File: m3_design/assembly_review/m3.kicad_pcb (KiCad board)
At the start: 4 copper layers, 46 x 193 mm, 232 parts, among them J1 BAT+ / GND / SW / SW, J120 ARM CH2: RAW / BUS2, J121 IGNITER 1: E1- / E1+, J122 SERVO 3x4, J123 PULL-PIN PH 1x2, J124 ARM CH1: BUS1 / RAW, J125 IGNITER 2: E2+ / E2-, J2 SWD 1x6, J3 USB-C 2.0, J9 CAM 5V / GND / RX / TX, Q120 AON6403, Q121 AON6403, Q122 AO3400A, Q123 AO3400A, Q124 AON7524, Q125 AON7524, U1 STM32H743VIT6, U10 TPS2553DBVR, U11 TPS2121RUXR, U12 TXU0202DCUR, U13 TPS70933DBVR, U2 AP63203WU-7, U3 W25Q128JVSIQ, U4 LSM6DSV320X, U5 MS561101BA03, U7 TPS259570DSGR, U8 AP63301WU-7, U9 TPS259470LRPWR, Y1 25MHz CL8pF

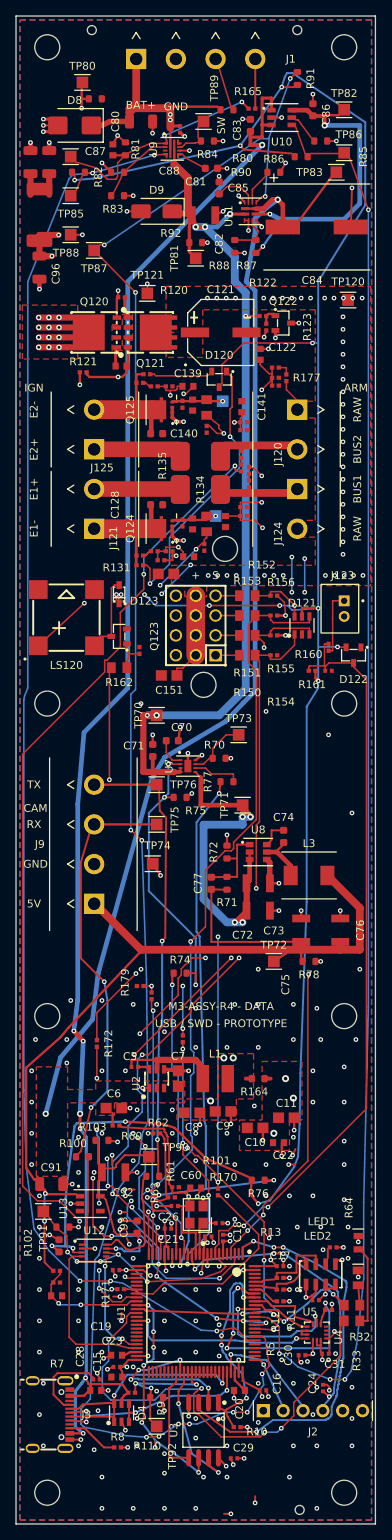
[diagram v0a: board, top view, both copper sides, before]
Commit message: M3-ASSY-R5: two-sided re-layout at 46 x 100 mm, fully routed
R4's schematic and BOM on a new board, parts on both sides (top 89 parts and
2 test pads, bottom 116 SMD parts and 22 test pads), generated from the R4
board by m3_design/r5_build.sh:
- r5_pcb.py / r5_routes.py / r5_maze.py: placement, zones and the scripted
  critical copper (USB, HSE, QSPI, SPI1, power paths, pyro block moved as one
  rigid group), plus the slow links the autorouter could not finish
- r5_route.py: Freerouting v2.4.1 export/import (session in git)
- r5_finish.py: what the router leaves, forced moves across non-critical
  copper, one hand-finish entry; its result is recorded in r5_finish.json and
  replayed, because KiCad's DRC does not list open connections the same way
  on every run
- r5_post.py: clean-up, stitching, return vias, silkscreen

tools/check.sh: DRC 0, unconnected 0, schematic parity 0, ERC 0, audit OK.
check_actuators.py OK; fit_check.py OK (worst margin C84 0.11 mm).
Docs: M3_R5.md, STATUS.md, ORDERING.md and REQUIREMENTS.md still carry
placeholders for the fab, cost and review results (next commits).

Co-Authored-By: Claude Opus 5.5 <noreply@anthropic.com>
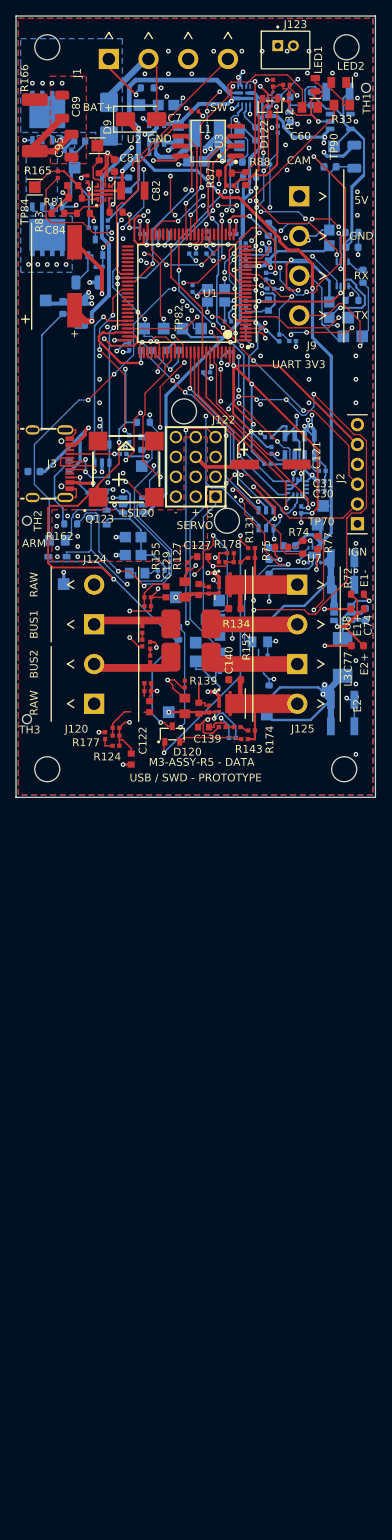
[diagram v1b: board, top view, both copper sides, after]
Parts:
- C10, C11, C120, C13, C14, C15, C150, C151, C16, C17, C18, C19, C20, C21, C22, C23, C24, C25, C26, C28, C30, C31, C32, C5, C6, C60, C7, C70, C71, C72, C73, C74, C75, C76, C8, C80, C83, C85, C86, C9, C90, C91, C92, C93, C94, C96, D121, D123, D4, D8, L1, L3, Q120, Q121, Q122, Q123, R100, R101, R102, R103, R104, R105, R11, R110, R12, R120, R121, R122, R123, R13, R150, R151, R152, R153, R154, R155, R156, R157, R162, R163, R164, R167, R168, R169, R170, R171, R172, R179, R5, R60, R61, R62, R63, R64, R7, R70, R76, R78, R8, R80, R85, R86, R9, R90, R91, R92, TP120, TP121, TP70, TP71, TP72, TP73, TP74, TP75, TP76, TP80, TP81, TP82, TP83, TP85, TP86, TP87, TP88, TP90, TP91, TP92, U10, U11, U12, U13, U2, U4, U5, U7, U8, Y1: moved to B.Cu
- moved C29 172.5 mm to (22.9, 12.2)
- moved U3 165.0 mm to (24.6, 16.0), turned to 90 degrees
- moved R10 158.9 mm to (27.4, 21.7)
- moved C94 156.2 mm to (34.4, 10.4)
- moved R32 155.4 mm to (37.6, 11.7)
- moved R33 153.6 mm to (41.7, 11.4)
- moved R105 153.4 mm to (32.2, 11.1), turned to 90 degrees
- moved LED2 153.0 mm to (41.3, 8.50), turned to 0 degrees
- moved R104 150.3 mm to (32.6, 12.8), turned to 180 degrees
- moved C16 148.8 mm to (16.3, 27.9)
- moved LED1 148.3 mm to (38.3, 8.80), turned to 90 degrees
- moved C24 146.4 mm to (29.4, 29.5)
- moved C15 145.8 mm to (27.8, 27.9), turned to 0 degrees
- moved C19 143.6 mm to (18.9, 27.9), turned to 0 degrees
- moved C90 142.4 mm to (40.2, 19.3), turned to 0 degrees
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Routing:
- net GND: track 167.1 -> 358.4 mm, vias 245 -> 122
- net LOGIC_SOURCE_ST: track 231.4 -> 54.9 mm, vias 13 -> 5
- net BAT_FAULT_N: track 184.0 -> 26.0 mm
- net VBUS: track 202.4 -> 48.7 mm, vias 7 -> 6
- net USB_FAULT_N: track 179.9 -> 31.8 mm, vias 4 -> 3
- net USB_LIMITED: track 40.7 -> 156.1 mm, vias 3 -> 2
- net PYRO1_GATE_N: track 120.9 -> 43.0 mm, vias 5 -> 2
- net CAM_5V: track 128.6 -> 51.0 mm, vias 2 -> 7
- net 3V3A: track 19.4 -> 96.6 mm, vias 8 -> 7
- net VLOGIC: track 144.8 -> 67.7 mm, vias 2 -> 7
- net ARM2_SENSE: track 134.0 -> 66.2 mm, vias 5 -> 3
- net PULLPIN: track 96.2 -> 37.9 mm, vias 2 -> 3
- net SERVO4_OUT: track 3.06 -> 57.2 mm, vias 0 -> 4
- net 3V3: track 343.1 -> 396.3 mm, vias 36 -> 34
- net PYRO2_GATE_N: track 119.3 -> 66.7 mm, vias 6 -> 2
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- added copper zone on B.Cu, net ACT_FET_S
- added copper zone on B.Cu, net BAT_IN
- added copper zone on In2.Cu, net CAM_5V
- added copper zone on B.Cu, net RAW_ACT
- removed copper zone on F.Cu, net 3V3
- removed copper zone on F.Cu, net 3V3A
- removed copper zone on F.Cu, net ACT_FET_S
- removed copper zone on F.Cu, net VLOGIC
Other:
- board size 46 x 193 mm -> 46 x 100 mm
- board text added: "2S INPUT / M3-ASSY-R5"
- board text added: "M3-ASSY-R5 - DATA"
- board text removed: "2S INPUT / M3-ASSY-R4"
- board text removed: "5V OUT"
- board text removed: "IGNITERS"
- board text removed: "M3-ASSY-R4 - DATA"
- board text removed: "RX CAM"
- board text removed: "TX CAM"

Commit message: M3-ASSY-R5: pass-1 fixes, re-routed (seed 81), nothing left open
Validation pass 1 fixes (M3_R5 section 1b, V1-V9): In2 keep-out under the
crystal, stitching vias off through-hole pads, U7 0.35 mm north, the MS5611
pad gap kept clear, J1 legends at their pins, bottom designators stay on the
bottom, more servo-feed vias at Q121, U9 escapes widened with a second OUT
via. C24's GND pad gets its own scripted 0.5 mm via (it or the reset pad was
boxed in in every routed board). The finisher records and replays its search
(r5_finish.json), with no hand-finish entries.

check.sh: DRC 0, unconnected 0, parity 0, ERC 0; actuator contract OK; fit OK.
Fab package regenerated: 84 lines, 205 placed, CPL rebuilt (the four residuals
are R4's); stock: no shortage, U4 thin; $79.93/board, targets met.

Co-Authored-By: Claude Opus 5.5 <noreply@anthropic.com>
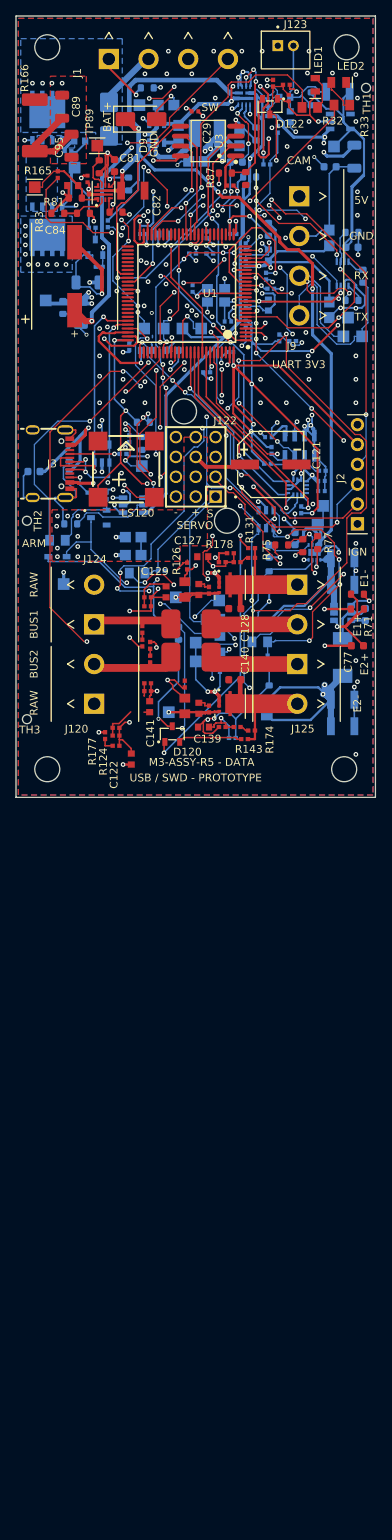
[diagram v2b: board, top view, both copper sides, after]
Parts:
- moved C71 1.14 mm to (35.7, 66.9), turned to 90 degrees
- moved U7 0.35 mm to (38.2, 68.7)
- moved C70 0.30 mm to (32.4, 68.5)
- moved R70 0.30 mm to (32.4, 71.9)
- moved R75 0.30 mm to (34.0, 67.7)
- moved R74 0.20 mm to (36.7, 67.8)
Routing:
- net SERVO3_OUT: track 32.8 -> 86.2 mm, vias 2 -> 9
- net CAM_ILIM: track 19.8 -> 49.4 mm
- net SERVO2_OUT: track 31.4 -> 59.3 mm, vias 1 -> 5
- net 3V3: track 396.3 -> 371.5 mm, vias 34 -> 33
- net USB_ILIM: track 31.5 -> 10.2 mm, vias 2 -> 0
- net SERVO3_MCU: track 95.3 -> 74.5 mm, vias 10 -> 9
- net NRST: track 57.4 -> 74.7 mm, vias 5 -> 6
- net BAT_FAULT_N: track 26.0 -> 42.0 mm, vias 5 -> 6
- net USB_OVLO: track 15.7 -> 29.2 mm, vias 1 -> 3
- net SERVO4_OUT: track 57.2 -> 44.9 mm, vias 4 -> 5
- net SWDIO: track 41.8 -> 53.9 mm, vias 6 -> 4
- net CAM_FAULT_N: track 112.6 -> 123.3 mm, vias 5 -> 6
- net CAM_PWR_EN: track 45.1 -> 55.0 mm, vias 2 -> 6
- net 3V3A: track 96.6 -> 88.7 mm, vias 7 -> 6
- net GND: track 358.4 -> 351.8 mm, vias 122 -> 132
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
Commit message: M3-ASSY-R5: validation pass 2 fixes
Pass 2 (six reviews on the re-routed board): no Critical, three Majors, fixed.
- D1: a router via inside J9.3's through-hole pad. r5_post.pth_vias removes
  vias on a through-hole pad of their own net (one removed).
- F1: M3_R5 section 3 had the IMU axes wrong. KiCad mirrors a bottom part in
  board y, so roll is +gyro_Y (opposite to R4). fit_check.py mirrors bottom
  models the same way; margins unchanged.
- S1: top designators moved to the bottom sat beside bottom parts; they now
  keep 1.2 mm from every bottom pad (83 hidden).
Minor findings corrected in the record (U9 OUT on one via, In2 reference under
U1, crystal keep-out text, USB length, ORDERING fees, D121 side, shroud and
nylon notes) or listed for the next revision in STATUS.md. M3_R5 sections 1c
and 5 filled; F4 DC solve 4.54 mOhm / 0.27 W.

check.sh: DRC 0, unconnected 0, parity 0, ERC 0; actuators OK; fit OK.

Co-Authored-By: Claude Opus 5.5 <noreply@anthropic.com>
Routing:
- net CAM_RX_WIRE: vias 2 -> 1
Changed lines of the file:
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@@
 		(tags "resistor")
 		(property "Reference" "R135"
-			(at 1.16128 -0.302373 90)
-			(layer "B.SilkS")
+			(at -5.796544 -0.200193 0)
+			(layer "F.SilkS")
 			(effects
 				(font
@@
 					(thickness 0.15)
 				)
-				(justify mirror)
 			)
 		)
@@
 		(descr "TI RPW0010A4225183/A; L-shaped lands via same-number union; external thermal vias")
 		(property "Reference" "U9"
-			(at 0.173206 -0.1 0)
+			(at 0 0 0)
 			(layer "B.SilkS")
 			(effects
@@
 		(tags "resistor")
 		(property "Reference" "R82"
-			(at -1 0 0)
+			(at 8.63 25.25 90)
 			(layer "B.SilkS")
+			(hide yes)
 			(effects
 				(font
@@
 		(at 23.4 88.6 90)
 		(property "Reference" "C138"
-			(at 0.173206 -0.100001 90)
+			(at 0.173206 0.1 90)
 			(layer "B.SilkS")
 			(effects
@@
 		(tags "resistor")
 		(property "Reference" "R84"
-			(at 0 0 0)
+			(at 0 0 90)
 			(layer "B.SilkS")
 			(effects
@@
 		(tags "capacitor")
 		(property "Reference" "C140"
-			(at -1.311543 2.473834 90)
-			(layer "F.SilkS")
+			(at 28 84.95 90)
+			(layer "B.SilkS")
+			(hide yes)
 			(effects
 				(font
@@
 					(thickness 0.15)
 				)
+				(justify mirror)
 			)
 		)
@@
 		(descr "BAT_ENABLE; Contact and UVLO divider measurement; >=10Mohm probe")
 		(property "Reference" "TP84"
-			(at -0.200001 -0.346411 0)
+			(at 0 0 0)
 			(layer "B.SilkS")
 			(effects
@@
 		(tags "capacitor")
 		(property "Reference" "C95"
-			(at -0.200533 -1.587384 90)
-			(layer "F.SilkS")
+			(at 16.6 -7.1 90)
+			(layer "B.SilkS")
+			(hide yes)
 			(effects
 				(font
@@
 					(thickness 0.15)
 				)
+				(justify mirror)
 			)
 		)
@@
 		(at 21.6 88.3 -90)
 		(property "Reference" "R138"
-			(at 0 0 90)
+			(at 0 -0.6 90)
 			(layer "B.SilkS")
 			(effects
@@
 		(tags "resistor 2512")
 		(property "Reference" "R166"
-			(at 6.06312 -1.295599 90)
+			(at -2.039756 2.465642 90)
 			(layer "F.SilkS")
 			(effects
@@
 		(tags "capacitor")
 		(property "Reference" "C128"
-			(at -1.311543 -2.473833 90)
-			(layer "F.SilkS")
+			(at 28 75.85 90)
+			(layer "B.SilkS")
+			(hide yes)
 			(effects
 				(font
@@
 					(thickness 0.15)
 				)
+				(justify mirror)
 			)
 		)
@@
 		(tags "resistor")
 		(property "Reference" "R134"
-			(at 22.4 77.8 90)
-			(layer "B.SilkS")
-			(hide yes)
+			(at -5.8 0 0)
+			(layer "F.SilkS")
 			(effects
 				(font
@@
 					(thickness 0.15)
 				)
-				(justify mirror)
 			)
 		)
@@
 		(descr "easyeda2kicad:SOT-23-3_L2.9-W1.3-P1.90-LS2.4-BR")
 		(property "Reference" "Q122"
-			(at 0.300799 2.381076 90)
+			(at 0.401446 -3.979804 0)
 			(layer "B.SilkS")
 			(effects
@@
 		(descr "100nF; VDD pin 75")
 		(property "Reference" "C16"
-			(at -1.369713 1.970758 0)
+			(at -16.3 -27.9 90)
 			(unlocked yes)
 			(layer "B.SilkS")
+			(hide yes)
 			(effects
 				(font
@@
 		(at 9.75 27.1)
 		(property "Reference" "R121"
-			(at -9.75 -27.1 90)
+			(at -1.549734 -0.397904 90)
 			(layer "B.SilkS")
-			(hide yes)
 			(effects
 				(font
@@
 		(at 11.75 26.6 -90)
 		(property "Reference" "R122"
-			(at -2.70185 1.714646 0)
+			(at -2.415211 1.77954 0)
 			(layer "B.SilkS")
 			(effects
@@
 		(at 4 27.3)
 		(property "Reference" "Q121"
-			(at -0.499753 -4.371527 0)
+			(at 3.499049 3.285826 90)
 			(layer "B.SilkS")
 			(effects
@@
 		(descr "GND; Power-entry test reference")
 		(property "Reference" "TP88"
-			(at -23 -82.6 90)
+			(at -2.798175 0.101086 0)
 			(layer "B.SilkS")
-			(hide yes)
 			(effects
 				(font
@@
 		(net "CAM_RX_WIRE")
 	)
-	(via
-		(at 37.2687 33.9777)
-		(size 0.6)
-		(drill 0.3)
-		(layers "F.Cu" "B.Cu")
-		(locked yes)
-		(net "CAM_RX_WIRE")
-	)

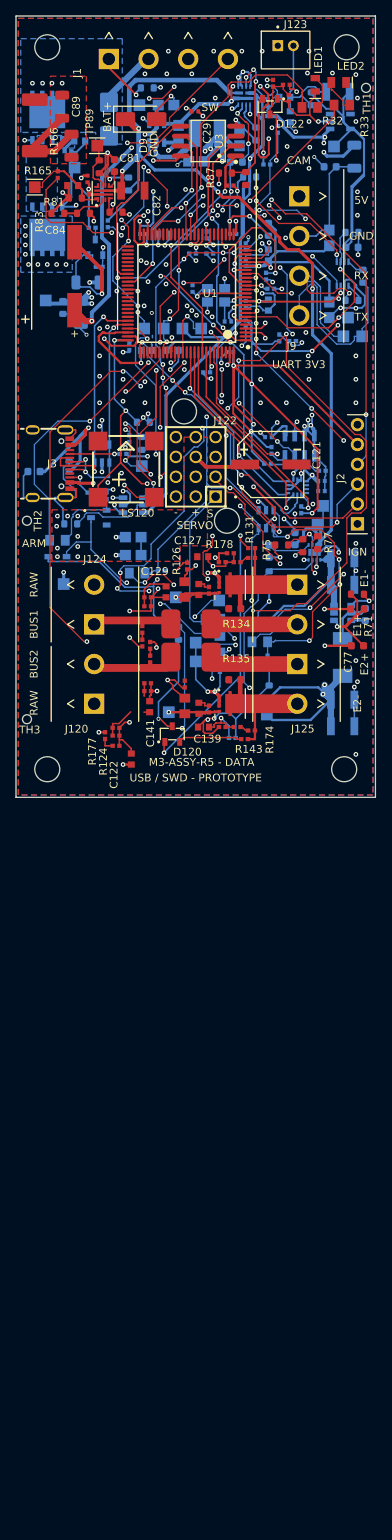
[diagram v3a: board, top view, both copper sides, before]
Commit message: M3-ASSY-R5: robustness round, re-routed (seed 61)
- B.Cu keep-out 1.0 mm round the bare gate test pads TP122/TP123 for the
  long links, autorouter and finisher: nearest live copper now 0.97 mm (was
  0.34 mm).
- Re-routed with Freerouting seed 61; the recorded finisher run drops a GND
  stub it left 0.12 mm from C14.1 and straightens a link that left an acute
  corner.
- J2's 3D model turned to lie along its pins.
- jlc_orient.py --verify-cpl applies the generator's pad filter and two-pad
  allowance; exits 0.

check.sh: DRC 0, unconnected 0, parity 0, ERC 0; actuators OK; fit OK.
DC solve 4.54 mOhm. Fab package regenerated.

Co-Authored-By: Claude Opus 5.5 <noreply@anthropic.com>
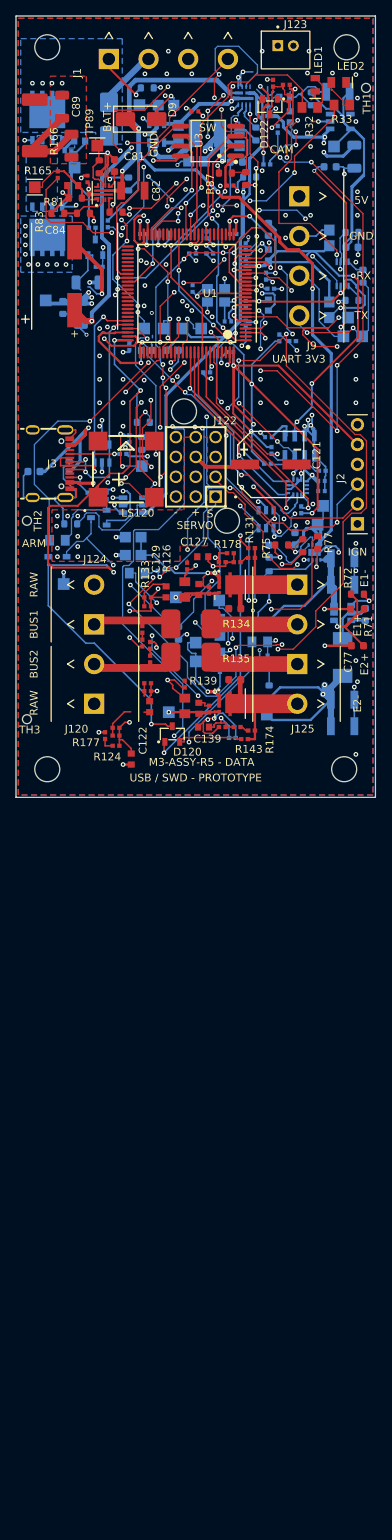
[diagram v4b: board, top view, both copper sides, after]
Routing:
- net CAM_FAULT_N: track 123.3 -> 75.7 mm
- net CAM_MCU_TX: track 30.1 -> 75.6 mm, vias 4 -> 8
- net PULLPIN: track 36.5 -> 78.7 mm, vias 2 -> 7
- net CAM_PWR_EN: track 55.0 -> 89.2 mm, vias 6 -> 8
- net CAM_ILIM: track 49.4 -> 23.0 mm
- net 3V3A: track 88.7 -> 103.0 mm, vias 6 -> 7
- net SERVO2_OUT: track 59.3 -> 71.9 mm, vias 5 -> 4
- net SERVO4_OUT: track 44.9 -> 32.3 mm, vias 5 -> 3
- net SERVO3_MCU: track 74.5 -> 61.9 mm, vias 9 -> 6
- net GND: track 351.8 -> 341.0 mm, vias 132 -> 130
- net CAM_5V_SENSE: track 50.0 -> 39.6 mm, vias 6 -> 7
- net CAM_UART_OE: track 29.1 -> 39.1 mm, vias 2 -> 3
- net SERVO1_MCU: track 107.3 -> 116.6 mm, vias 7 -> 8
- net 3V3: track 371.5 -> 362.4 mm, vias 33 -> 31
- net CAM_TX_WIRE: track 25.3 -> 17.9 mm, vias 0 -> 2
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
